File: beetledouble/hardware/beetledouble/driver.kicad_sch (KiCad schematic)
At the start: 19 parts, among them J5 motor_out, Q3 SE3082G, Q4 SE3082G, U6 NCP81155MN, U7 NCP81155MN

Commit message: update pcb
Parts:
- renumbered C14 to C11, C15 to C12, C16 to C13, C18 to C17, C5 to C3, C6 to C4, D5 to D3, D6 to D4, J5 to J4, Q3 to Q1, Q4 to Q2, R5 to R1, R6 to R2, R7 to R3, R8 to R4, U6 to U4, U7 to U5
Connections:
- net MOTORS1: no longer C3.2, U4.7 (SW)
- new net: C3.2, U4.7 (SW)
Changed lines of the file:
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@@
-    (effects (font (size 1.27 1.27)) (justify right bottom))
-  )
-  (label "MOTORS1" (at 71.755 100.33 180)
     (effects (font (size 1.27 1.27)) (justify right bottom))
   )
@@
   )
   (label "BOOST2" (at 73.66 139.7 180)
+    (effects (font (size 1.27 1.27)) (justify right bottom))
+  )
+  (label "MOTORS1" (at 74.295 100.33 180)
     (effects (font (size 1.27 1.27)) (justify right bottom))
   )
@@
   (symbol (lib_id "power:+12V") (at 52.705 72.39 0)
     (in_bom yes) (on_board yes)
-    (property "Reference" "#PWR012" (id 0) (at 52.705 76.2 0)
+    (property "Reference" "#PWR08" (id 0) (at 52.705 76.2 0)
       (effects (font (size 1.27 1.27)) hide)
     )
@@
   (symbol (lib_id "power:+12V") (at 52.705 135.89 0)
     (in_bom yes) (on_board yes)
-    (property "Reference" "#PWR010" (id 0) (at 52.705 139.7 0)
+    (property "Reference" "#PWR06" (id 0) (at 52.705 139.7 0)
       (effects (font (size 1.27 1.27)) hide)
     )
@@
   (symbol (lib_id "power:GND") (at 52.705 115.57 0)
     (in_bom yes) (on_board yes)
-    (property "Reference" "#PWR013" (id 0) (at 52.705 121.92 0)
+    (property "Reference" "#PWR09" (id 0) (at 52.705 121.92 0)
       (effects (font (size 1.27 1.27)) hide)
     )
@@
   (symbol (lib_id "power:GND") (at 52.705 177.165 0)
     (in_bom yes) (on_board yes)
-    (property "Reference" "#PWR011" (id 0) (at 52.705 183.515 0)
+    (property "Reference" "#PWR07" (id 0) (at 52.705 183.515 0)
       (effects (font (size 1.27 1.27)) hide)
     )
@@
   (symbol (lib_id "Device:R") (at 80.01 154.94 90)
     (in_bom yes) (on_board yes)
-    (property "Reference" "R5" (id 0) (at 80.01 149.7138 90))
+    (property "Reference" "R1" (id 0) (at 80.01 149.7138 90))
     (property "Value" "10R" (id 1) (at 80.01 152.0125 90))
     (property "Footprint" "Resistor_SMD:R_0603_1608Metric" (id 2) (at 80.01 156.718 90)
@@
   (symbol (lib_id "Device:R") (at 80.01 162.56 90)
     (in_bom yes) (on_board yes)
-    (property "Reference" "R6" (id 0) (at 80.01 157.3338 90))
+    (property "Reference" "R2" (id 0) (at 80.01 157.3338 90))
     (property "Value" "10R" (id 1) (at 80.01 159.6325 90))
     (property "Footprint" "Resistor_SMD:R_0603_1608Metric" (id 2) (at 80.01 164.338 90)
@@
   (symbol (lib_id "Device:R") (at 83.185 96.52 90)
     (in_bom yes) (on_board yes)
-    (property "Reference" "R7" (id 0) (at 83.185 91.2938 90))
+    (property "Reference" "R3" (id 0) (at 83.185 91.2938 90))
     (property "Value" "10R" (id 1) (at 83.185 93.5925 90))
     (property "Footprint" "Resistor_SMD:R_0603_1608Metric" (id 2) (at 83.185 98.298 90)
@@
   (symbol (lib_id "Device:R") (at 83.185 104.14 90)
     (in_bom yes) (on_board yes)
-    (property "Reference" "R8" (id 0) (at 83.185 98.9138 90))
+    (property "Reference" "R4" (id 0) (at 83.185 98.9138 90))
     (property "Value" "10R" (id 1) (at 83.185 101.2125 90))
     (property "Footprint" "Resistor_SMD:R_0603_1608Metric" (id 2) (at 83.185 105.918 90)
@@
   (symbol (lib_id "Connector:Conn_01x02_Female") (at 231.775 78.105 90)
     (in_bom yes) (on_board yes)
-    (property "Reference" "J5" (id 0) (at 236.4487 79.648 90)
+    (property "Reference" "J4" (id 0) (at 236.4487 79.648 90)
       (effects (font (size 1.27 1.27)) (justify right))
     )
@@
   (symbol (lib_id "Device:D_Schottky") (at 56.515 80.01 180)
     (in_bom yes) (on_board yes) (fields_autoplaced)
-    (property "Reference" "D5" (id 0) (at 56.515 74.93 0))
+    (property "Reference" "D3" (id 0) (at 56.515 74.93 0))
     (property "Value" "B5819W" (id 1) (at 56.515 77.47 0))
     (property "Footprint" "Diode_SMD:D_SOD-123" (id 2) (at 56.515 80.01 0)
@@
   (symbol (lib_id "Device:D_Schottky") (at 59.055 139.7 180)
     (in_bom yes) (on_board yes) (fields_autoplaced)
-    (property "Reference" "D6" (id 0) (at 59.055 134.62 0))
+    (property "Reference" "D4" (id 0) (at 59.055 134.62 0))
     (property "Value" "B5819W" (id 1) (at 59.055 137.16 0))
     (property "Footprint" "Diode_SMD:D_SOD-123" (id 2) (at 59.055 139.7 0)
@@
   (symbol (lib_id "Device:C") (at 73.66 87.63 0)
     (in_bom yes) (on_board yes)
-    (property "Reference" "C5" (id 0) (at 76.5811 86.4806 0)
+    (property "Reference" "C3" (id 0) (at 76.5811 86.4806 0)
       (effects (font (size 1.27 1.27)) (justify left))
     )
@@
   (symbol (lib_id "Device:C") (at 73.66 146.05 0)
     (in_bom yes) (on_board yes)
-    (property "Reference" "C6" (id 0) (at 76.581 144.901 0)
+    (property "Reference" "C4" (id 0) (at 76.581 144.901 0)
       (effects (font (size 1.27 1.27)) (justify left))
     )
@@
   (symbol (lib_id "Device:C") (at 158.75 85.09 0)
     (in_bom yes) (on_board yes)
-    (property "Reference" "C14" (id 0) (at 161.6711 83.9406 0)
+    (property "Reference" "C11" (id 0) (at 161.6711 83.9406 0)
       (effects (font (size 1.27 1.27)) (justify left))
     )
@@
   (symbol (lib_id "Device:C") (at 170.18 85.09 0)
     (in_bom yes) (on_board yes)
-    (property "Reference" "C15" (id 0) (at 173.1011 83.9406 0)
+    (property "Reference" "C12" (id 0) (at 173.1011 83.9406 0)
       (effects (font (size 1.27 1.27)) (justify left))
     )
@@
   (symbol (lib_id "Device:C") (at 179.705 85.09 0)
     (in_bom yes) (on_board yes)
-    (property "Reference" "C16" (id 0) (at 180.0861 82.6706 0)
+    (property "Reference" "C13" (id 0) (at 180.0861 82.6706 0)
       (effects (font (size 1.27 1.27)) (justify left))
     )
@@
   (symbol (lib_id "Device:C") (at 186.055 85.09 0)
     (in_bom yes) (on_board yes)
-    (property "Reference" "C18" (id 0) (at 187.0711 82.0356 0)
+    (property "Reference" "C17" (id 0) (at 187.0711 82.0356 0)
       (effects (font (size 1.27 1.27)) (justify left))
     )
@@
   (symbol (lib_id "Device:Q_Dual_PMOS_S1G1S2G2D2D2D1D1") (at 208.28 78.74 0)
     (in_bom yes) (on_board yes) (fields_autoplaced)
-    (property "Reference" "Q3" (id 0) (at 215.265 78.1049 0)
+    (property "Reference" "Q1" (id 0) (at 215.265 78.1049 0)
       (effects (font (size 1.27 1.27)) (justify left))
     )
@@
   (symbol (lib_id "Device:Q_Dual_PMOS_S1G1S2G2D2D2D1D1") (at 208.28 92.075 0)
     (in_bom yes) (on_board yes) (fields_autoplaced)
-    (property "Reference" "Q3" (id 0) (at 214.63 91.4399 0)
+    (property "Reference" "Q1" (id 0) (at 214.63 91.4399 0)
       (effects (font (size 1.27 1.27)) (justify left))
     )
@@
     )
     (property "LCSC" "C238670" (id 4) (at 208.28 92.075 0)
+      (effects (font (size 1.27 1.27)) hide)
+    )
+    (pin "3")
+    (pin "4")
+    (pin "5")
+    (pin "6")
+  )
+  (symbol (lib_id "Device:Q_Dual_PMOS_S1G1S2G2D2D2D1D1") (at 256.54 78.74 0)
+    (in_bom yes) (on_board yes) (fields_autoplaced)
+    (property "Reference" "Q2" (id 0) (at 263.525 78.1049 0)
+      (effects (font (size 1.27 1.27)) (justify left))
+    )
+    (property "Value" "SE3082G" (id 1) (at 263.525 80.6449 0)
+      (effects (font (size 1.27 1.27)) (justify left))
+    )
+    (property "Footprint" "beetledouble:Infineon-PG-TDSON" (id 2) (at 257.81 78.74 0)
+      (effects (font (size 1.27 1.27)) hide)
+    )
+    (property "Datasheet" "~" (id 3) (at 257.81 78.74 0)
+      (effects (font (size 1.27 1.27)) hide)
+    )
+    (property "LCSC" "C238670" (id 4) (at 256.54 78.74 0)
       (effects (font (size 1.27 1.27)) hide)
     )
@@
     (pin "8")
   )
-  (symbol (lib_id "Device:Q_Dual_PMOS_S1G1S2G2D2D2D1D1") (at 256.54 78.74 0)
-    (in_bom yes) (on_board yes) (fields_autoplaced)
-    (property "Reference" "Q4" (id 0) (at 263.525 78.1049 0)
-      (effects (font (size 1.27 1.27)) (justify left))
-    )
-    (property "Value" "SE3082G" (id 1) (at 263.525 80.6449 0)
-      (effects (font (size 1.27 1.27)) (justify left))
-    )
-    (property "Footprint" "beetledouble:Infineon-PG-TDSON" (id 2) (at 257.81 78.74 0)
-      (effects (font (size 1.27 1.27)) hide)
-    )
-    (property "Datasheet" "~" (id 3) (at 257.81 78.74 0)
-      (effects (font (size 1.27 1.27)) hide)
-    )
-    (property "LCSC" "C238670" (id 4) (at 256.54 78.74 0)
-      (effects (font (size 1.27 1.27)) hide)
-    )
-    (pin "1")
-    (pin "2")
-    (pin "7")
-    (pin "8")
-  )
   (symbol (lib_id "Device:Q_Dual_PMOS_S1G1S2G2D2D2D1D1") (at 256.54 92.075 0)
     (in_bom yes) (on_board yes) (fields_autoplaced)
-    (property "Reference" "Q4" (id 0) (at 262.89 91.4399 0)
+    (property "Reference" "Q2" (id 0) (at 262.89 91.4399 0)
       (effects (font (size 1.27 1.27)) (justify left))
     )
@@
       (effects (font (size 1.27 1.27)) hide)
     )
-    (pin "1")
-    (pin "2")
-    (pin "7")
-    (pin "8")
+    (pin "3")
+    (pin "4")
+    (pin "5")
+    (pin "6")
   )
   (symbol (lib_id "beetledouble:NCP81155MN") (at 52.705 100.33 0)
     (in_bom yes) (on_board yes)
-    (property "Reference" "U6" (id 0) (at 44.1325 90.17 0))
+    (property "Reference" "U4" (id 0) (at 44.1325 90.17 0))
     (property "Value" "NCP81155MN" (id 1) (at 44.1325 87.63 0))
     (property "Footprint" "beetledouble:DFN-8-3x3mm_hand1" (id 2) (at 52.705 100.33 0)
@@
   (symbol (lib_id "beetledouble:NCP81155MN") (at 52.705 158.75 0)
     (in_bom yes) (on_board yes)
-    (property "Reference" "U7" (id 0) (at 44.1325 148.59 0))
+    (property "Reference" "U5" (id 0) (at 44.1325 148.59 0))
     (property "Value" "NCP81155MN" (id 1) (at 44.1325 146.05 0))
     (property "Footprint" "beetledouble:DFN-8-3x3mm_hand1" (id 2) (at 52.705 158.75 0)

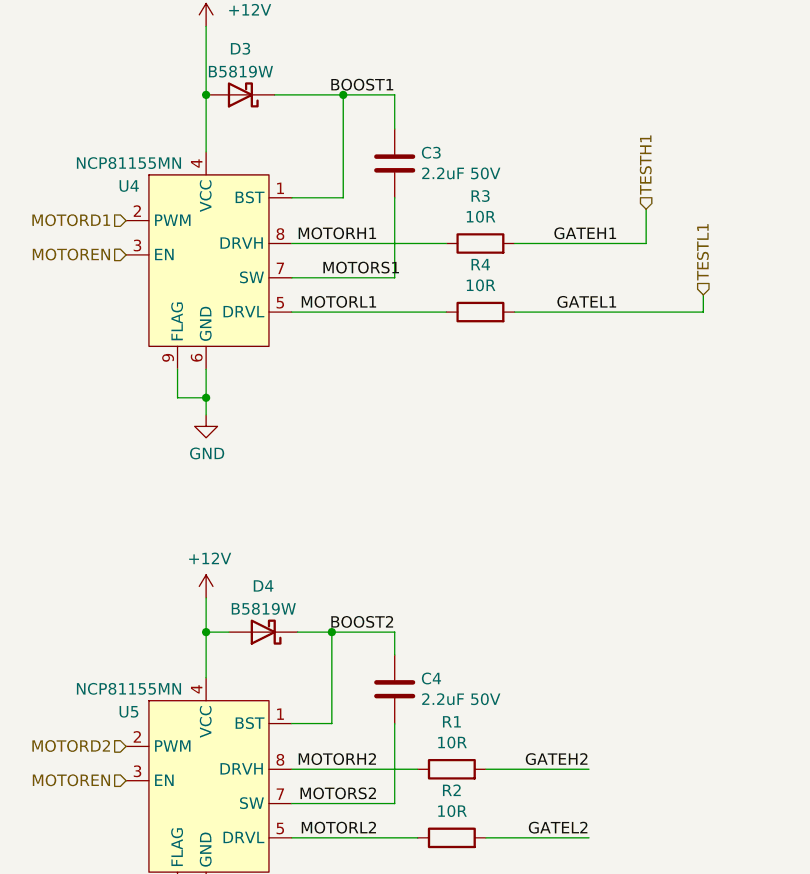
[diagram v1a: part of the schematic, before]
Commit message: Minor pcb tweaks for better reliability solderability etc
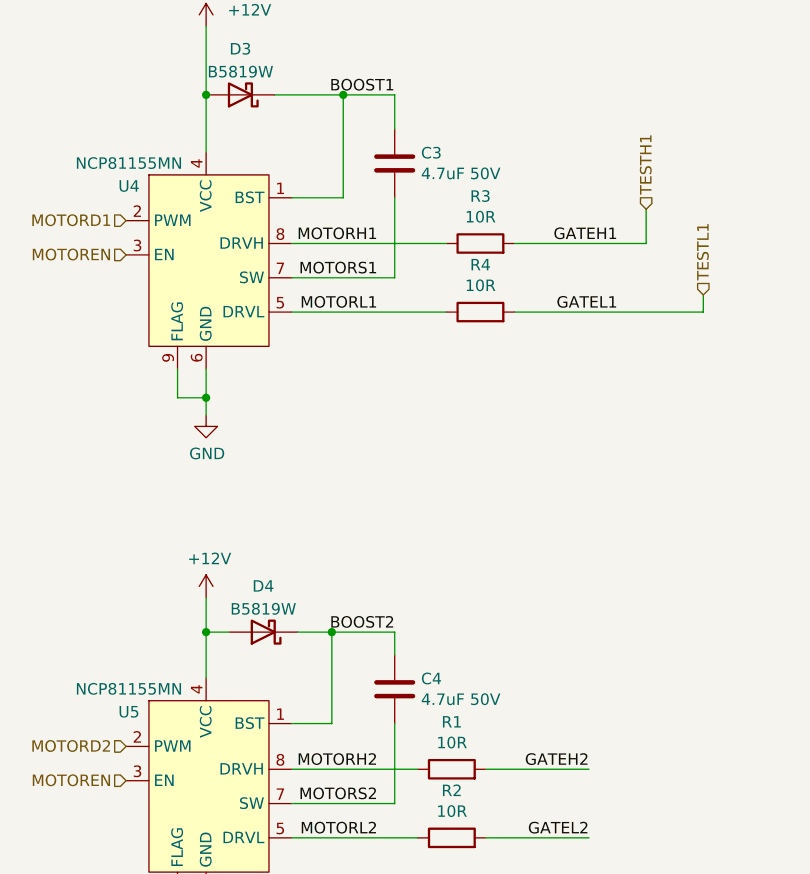
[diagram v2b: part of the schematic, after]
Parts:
- C3, C4: value 2.2uF 50V -> 4.7uF 50V; footprint Capacitor_SMD:C_0603_1608Metric -> Capacitor_SMD:C_0603_1608Metric_Pad1.08x0.95mm_HandSolder
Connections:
- net MOTORS1: now also C3.2, U4.7 (SW)
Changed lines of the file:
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@@
+    (effects (font (size 1.27 1.27)) (justify right bottom))
+  )
+  (label "MOTORS1" (at 71.755 100.33 180)
     (effects (font (size 1.27 1.27)) (justify right bottom))
   )
@@
   )
   (label "BOOST2" (at 73.66 139.7 180)
-    (effects (font (size 1.27 1.27)) (justify right bottom))
-  )
-  (label "MOTORS1" (at 74.295 100.33 180)
     (effects (font (size 1.27 1.27)) (justify right bottom))
   )
@@
       (effects (font (size 1.27 1.27)) (justify left))
     )
-    (property "Value" "2.2uF 50V" (id 1) (at 76.5811 88.7793 0)
-      (effects (font (size 1.27 1.27)) (justify left))
-    )
-    (property "Footprint" "Capacitor_SMD:C_0603_1608Metric" (id 2) (at 74.6252 91.44 0)
+    (property "Value" "4.7uF 50V" (id 1) (at 76.5811 88.7793 0)
+      (effects (font (size 1.27 1.27)) (justify left))
+    )
+    (property "Footprint" "Capacitor_SMD:C_0603_1608Metric_Pad1.08x0.95mm_HandSolder" (id 2) (at 74.6252 91.44 0)
       (effects (font (size 1.27 1.27)) hide)
     )
@@
       (effects (font (size 1.27 1.27)) (justify left))
     )
-    (property "Value" "2.2uF 50V" (id 1) (at 76.5811 147.1993 0)
-      (effects (font (size 1.27 1.27)) (justify left))
-    )
-    (property "Footprint" "Capacitor_SMD:C_0603_1608Metric" (id 2) (at 74.6252 149.86 0)
-      (effects (font (size 1.27 1.27)) hide)
-    )
+    (property "Value" "4.7uF 50V" (id 1) (at 76.5811 147.1993 0)
+      (effects (font (size 1.27 1.27)) (justify left))
+    )
+    (property "Footprint" "Capacitor_SMD:C_0603_1608Metric_Pad1.08x0.95mm_HandSolder" (id 2) (at 74.6252 149.86 0)
+      (effects (font (size 1.27 1.27)) hide)
+    )
